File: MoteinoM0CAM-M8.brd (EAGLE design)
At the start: 22.6 x 22.2 mm, 9 parts

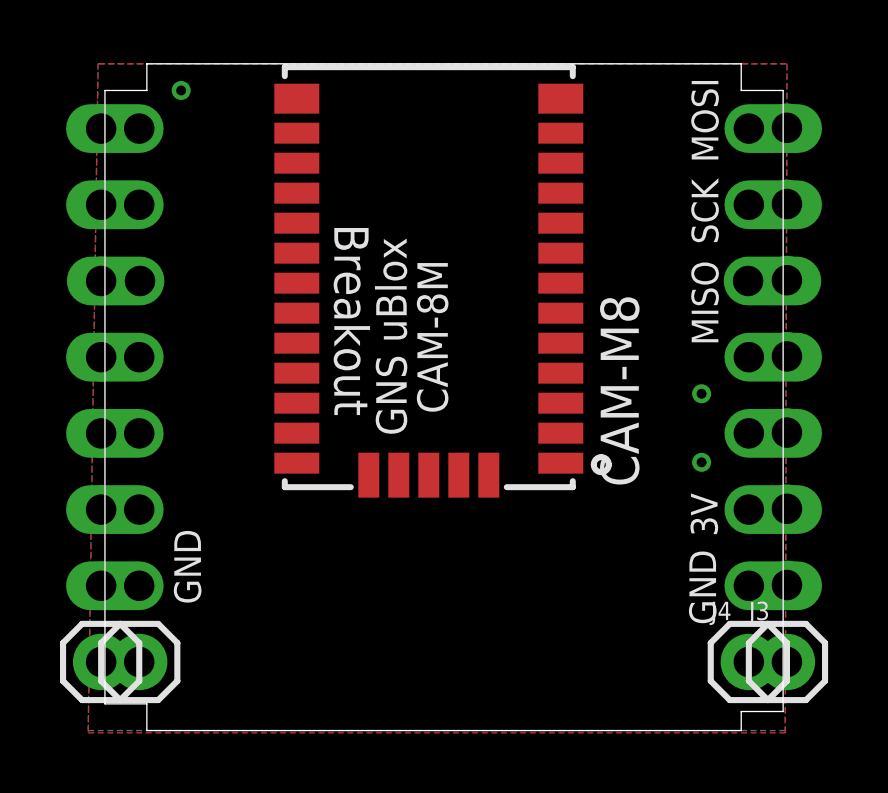
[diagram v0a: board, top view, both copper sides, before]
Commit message: Added resistors, led and capacitors
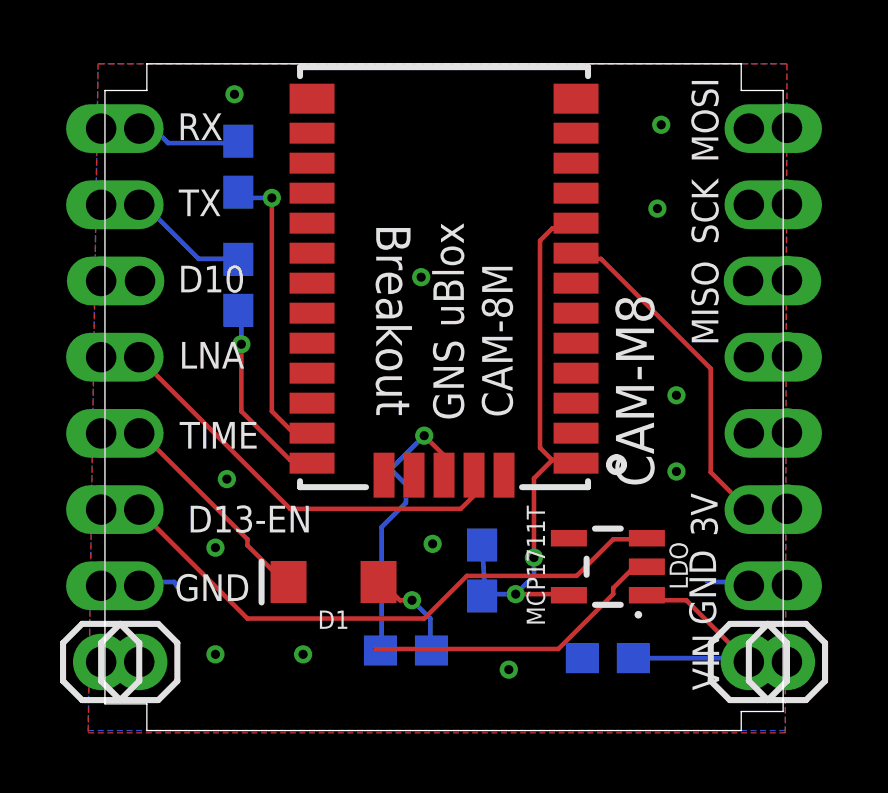
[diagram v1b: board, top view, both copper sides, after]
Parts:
- added C1, C2: 100n, SparkFun-Capacitors:0603
- added D1: GREEN, SparkFun-LED:LED-1206
- added LDO: MCP1711T, SparkFun-IC-Power:SOT23-5
- added R1, R2, R3: 220, SparkFun-Resistors:0603
- moved U$1 0.51 mm to (11.4, 13.2)
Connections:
- removed net D11: U$17.4
- removed net D12: U$17.3
- removed net D13: U$17.2
- new net D11_LNA_EN: U$1.30, U$17.4
- new net D12_TIMEPULSE: D1.C, U$17.3
- new net D13_ENABLE: LDO.3, U$17.2
- new net N$1: R3.2, U$1.29
- new net N$3: R2.2, U$1.26
- new net N$4: D1.A, R3.1
- new net VCC: C2.1, LDO.5, U$1.1, U$1.9
- net GND: now also C1.2, C2.2, LDO.2
- net N$2: now also R1.2, U$1.25; no longer U$1.1, U$1.9
- net PB22/TXD: now also R2.1
- net PB23/RXD: now also R1.1
- net VIN: now also C1.1, LDO.1
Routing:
- net D13_ENABLE: track 0.00 -> 19.5 mm
- net VCC: track 0.00 -> 19.2 mm, vias 0 -> 2
- net D11_LNA_EN: track 0.00 -> 14.1 mm
- net GND: track 0.00 -> 13.5 mm, vias 3 -> 12
- net 3.3V: track 0.00 -> 11.4 mm
- net N$1: track 0.00 -> 10.3 mm, vias 0 -> 1
- net N$2: track 0.00 -> 9.99 mm, vias 0 -> 1
- net VIN: track 0.00 -> 8.47 mm
- net D12_TIMEPULSE: track 0.00 -> 7.13 mm
- net N$3: track 0.00 -> 6.47 mm, vias 0 -> 1
- net PB22/TXD: track 0.00 -> 4.06 mm
- net PB23/RXD: track 0.00 -> 3.51 mm
- net N$4: track 0.00 -> 3.31 mm, vias 0 -> 1
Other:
- board text added: "D10"
- board text added: "D13-EN"
- board text added: "LNA"
- board text added: "RX"
- board text added: "TIME"
- board text added: "TX"
- board text added: "VIN"

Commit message: Doco update III
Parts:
- C1, C2: value 100n -> 100nF
- moved D1 3.74 mm to (5.59, 0.00)
- moved R3 2.88 mm to (8.00, 2.67), flipped to the top
- moved C2 0.76 mm to (12.7, 2.67), flipped to the top
- moved C1 0.51 mm to (16.9, 0.00), flipped to the top
- moved LDO 0.51 mm to (16.9, 3.05)
- flipped R1 to the top
- flipped R2 to the top
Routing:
- net GND: track 13.5 -> 23.9 mm, vias 12 -> 0
- net D13_ENABLE: track 19.5 -> 25.3 mm
- net N$1: track 10.3 -> 4.98 mm, vias 1 -> 0
- net D12_TIMEPULSE: track 7.13 -> 9.21 mm
- net VCC: track 19.2 -> 17.5 mm, vias 2 -> 0
- net VIN: track 8.47 -> 7.11 mm
- net N$4: track 3.31 -> 2.71 mm, vias 1 -> 0
- net N$2: track 9.99 -> 9.39 mm, vias 1 -> 0
- net N$3: vias 1 -> 0
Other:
- board text added: "CAM-M8Q"
- board text removed: "CAM-M8"

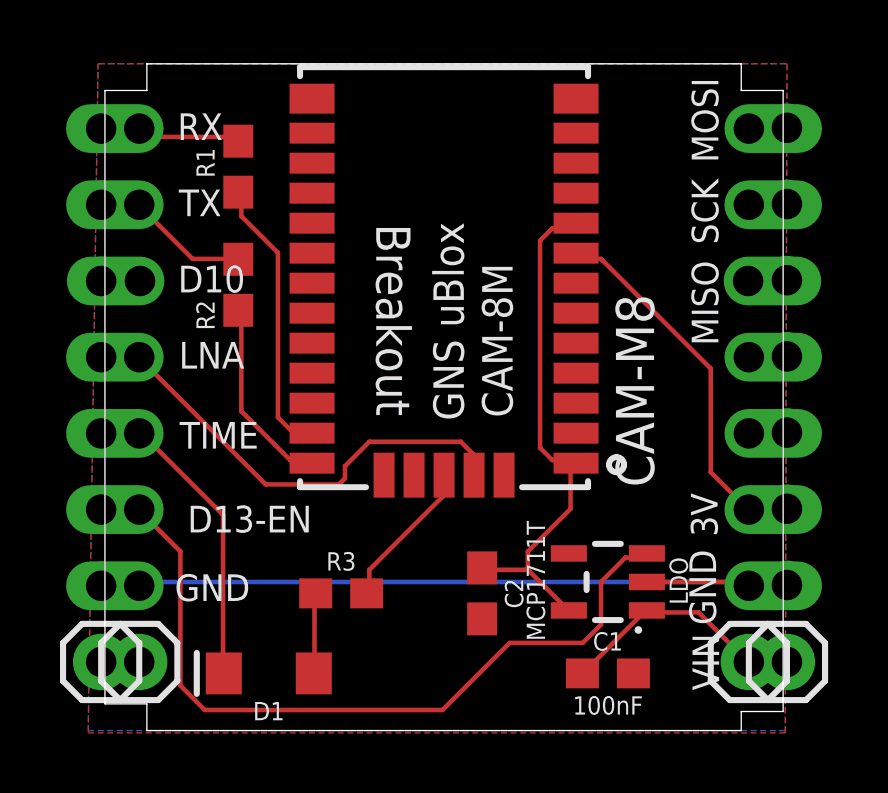
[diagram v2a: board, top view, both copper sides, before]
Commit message: Added images
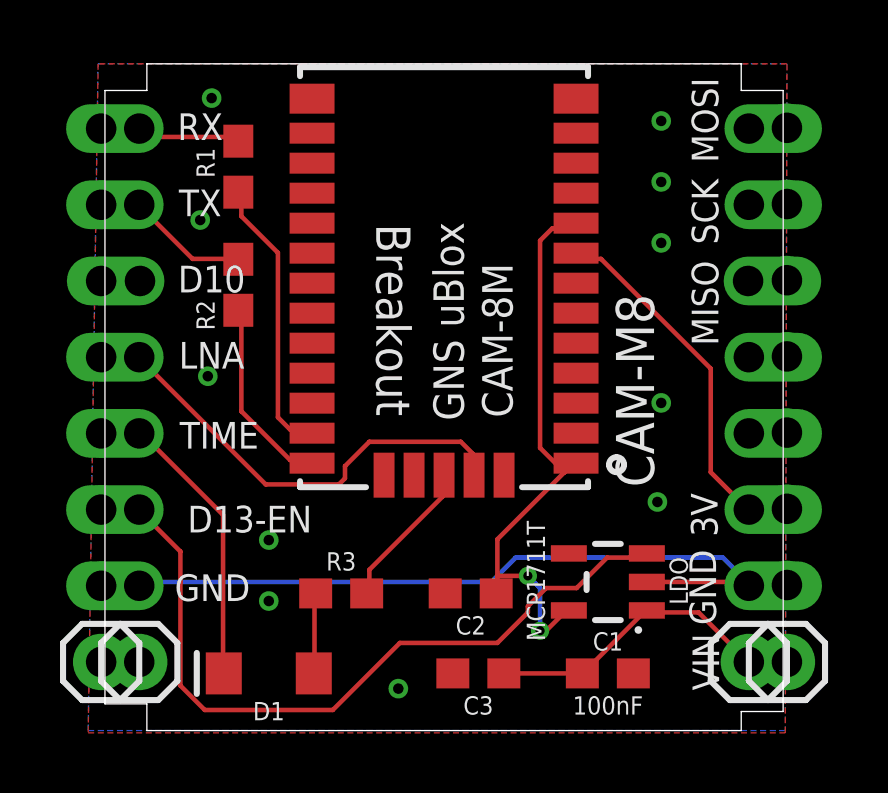
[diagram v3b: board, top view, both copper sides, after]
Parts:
- added C3: 4.7uF, SparkFun-Capacitors:0603
- moved C2 0.38 mm to (12.3, 2.67), turned to 180 degrees
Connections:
- net GND: now also C3.2
- net VIN: now also C3.1
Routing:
- net VIN: track 7.11 -> 9.73 mm
- net VCC: track 17.5 -> 19.7 mm, vias 0 -> 2
- net D13_ENABLE: track 25.3 -> 24.6 mm
- net GND: track 23.9 -> 24.6 mm, vias 0 -> 11
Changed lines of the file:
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@@
 <attribute name="VALUE" x="16.891" y="-0.762" size="0.6096" layer="25" font="vector" ratio="20" align="top-center"/>
 </element>
-<element name="C2" library="SparkFun-Capacitors" library_urn="urn:adsk.eagle:library:510" package="0603" package3d_urn="urn:adsk.eagle:package:37414/1" value="100nF" x="12.7" y="2.667" smashed="yes" rot="R270">
-<attribute name="NAME" x="13.462" y="2.667" size="0.6096" layer="25" font="vector" ratio="20" rot="R270" align="bottom-center"/>
-<attribute name="PROD_ID" value="CAP-08604" x="12.7" y="2.667" size="1.778" layer="27" rot="R270" display="off"/>
-<attribute name="VALUE" x="11.938" y="2.667" size="0.6096" layer="27" font="vector" ratio="20" rot="R270" align="top-center"/>
+<element name="C2" library="SparkFun-Capacitors" library_urn="urn:adsk.eagle:library:510" package="0603" package3d_urn="urn:adsk.eagle:package:37414/1" value="100nF" x="12.319" y="2.667" smashed="yes" rot="R180">
+<attribute name="NAME" x="12.319" y="1.905" size="0.6096" layer="25" font="vector" ratio="20" rot="R180" align="bottom-center"/>
+<attribute name="PROD_ID" value="CAP-08604" x="12.319" y="2.667" size="1.778" layer="27" rot="R180" display="off"/>
+<attribute name="VALUE" x="12.319" y="3.429" size="0.6096" layer="27" font="vector" ratio="20" rot="R180" align="top-center"/>
 </element>
 <element name="D1" library="SparkFun-LED" library_urn="urn:adsk.eagle:library:529" package="LED-1206" package3d_urn="urn:adsk.eagle:package:39352/1" value="GREEN" x="5.588" y="0" smashed="yes" rot="R180">
@@
 <attribute name="PROD_ID" value="RES-07861" x="8.001" y="2.667" size="1.778" layer="27" display="off"/>
 <attribute name="VALUE" x="8.001" y="1.905" size="0.6096" layer="27" font="vector" ratio="20" align="top-center"/>
+</element>
+<element name="C3" library="SparkFun-Capacitors" library_urn="urn:adsk.eagle:library:510" package="0603" package3d_urn="urn:adsk.eagle:package:37414/1" value="4.7uF" x="12.573" y="0" smashed="yes" rot="R180">
+<attribute name="NAME" x="12.573" y="-0.762" size="0.6096" layer="25" font="vector" ratio="20" rot="R180" align="bottom-center"/>
+<attribute name="PROD_ID" value="CAP-08280" x="12.573" y="0" size="1.778" layer="27" rot="R180" display="off"/>
+<attribute name="VALUE" x="12.573" y="0.762" size="0.6096" layer="27" font="vector" ratio="20" rot="R180" align="top-center"/>
 </element>
 </elements>
@@
 <contactref element="C2" pad="2"/>
 <contactref element="U$18" pad="1"/>
-<wire x1="21.5392" y1="3.048" x2="1.4224" y2="3.048" width="0.1524" layer="16"/>
+<contactref element="C3" pad="2"/>
+<wire x1="13.0048" y1="3.048" x2="1.4224" y2="3.048" width="0.1524" layer="16"/>
+<wire x1="13.8176" y1="3.8608" x2="13.0048" y2="3.048" width="0.1524" layer="16"/>
+<wire x1="20.7264" y1="3.8608" x2="13.8176" y2="3.8608" width="0.1524" layer="16"/>
+<wire x1="21.5392" y1="3.048" x2="20.7264" y2="3.8608" width="0.1524" layer="16"/>
 <wire x1="1.4224" y1="3.048" x2="1.27" y2="2.921" width="0.1524" layer="16"/>
 <wire x1="21.5392" y1="3.048" x2="21.59" y2="2.921" width="0.1524" layer="16"/>
 <wire x1="18.1911" y1="3.048" x2="21.5392" y2="3.048" width="0.1524" layer="1"/>
 <wire x1="21.5392" y1="3.048" x2="21.59" y2="2.921" width="0.1524" layer="1"/>
-<wire x1="13.43" y1="6.608" x2="9.43" y2="6.608" width="0" layer="19" extent="1-1"/>
-<wire x1="15.83" y1="10.008" x2="13.43" y2="6.608" width="0" layer="19" extent="1-1"/>
-<wire x1="17.741" y1="0" x2="18.1911" y2="3.048" width="0" layer="19" extent="1-1"/>
-<wire x1="15.83" y1="16.008" x2="15.83" y2="11.008" width="0" layer="19" extent="1-1"/>
+<via x="3.683" y="19.177" extent="1-16" drill="0.35"/>
+<via x="3.302" y="15.113" extent="1-16" drill="0.35"/>
+<via x="3.556" y="9.906" extent="1-16" drill="0.35"/>
+<via x="5.588" y="4.445" extent="1-16" drill="0.35"/>
+<via x="5.588" y="2.413" extent="1-16" drill="0.35"/>
+<via x="9.906" y="-0.508" extent="1-16" drill="0.35"/>
+<via x="18.542" y="5.715" extent="1-16" drill="0.35"/>
+<via x="18.669" y="9.017" extent="1-16" drill="0.35"/>
+<via x="18.669" y="14.351" extent="1-16" drill="0.35"/>
+<via x="18.669" y="16.383" extent="1-16" drill="0.35"/>
+<via x="18.669" y="18.415" extent="1-16" drill="0.35"/>
+<wire x1="18.669" y1="16.383" x2="18.669" y2="18.415" width="0" layer="19" extent="1-1"/>
+<wire x1="11.469" y1="2.667" x2="13.0048" y2="3.048" width="0" layer="19" extent="1-16"/>
 </signal>
 <signal name="SDA">
@@
 <contactref element="LDO" pad="1"/>
 <contactref element="C1" pad="1"/>
-<wire x1="18.0848" y1="2.032" x2="16.0528" y2="0" width="0.1524" layer="1"/>
+<contactref element="C3" pad="1"/>
+<wire x1="16.041" y1="0" x2="13.423" y2="0" width="0.1524" layer="1"/>
+<wire x1="16.0528" y1="0" x2="18.0848" y2="2.032" width="0.1524" layer="1"/>
+<wire x1="18.0848" y1="2.032" x2="18.1911" y2="2.098" width="0.1524" layer="1"/>
 <wire x1="16.0528" y1="0" x2="16.041" y2="0" width="0.1524" layer="1"/>
-<wire x1="18.0848" y1="2.032" x2="18.1911" y2="2.098" width="0.1524" layer="1"/>
 <wire x1="19.9136" y1="2.032" x2="18.288" y2="2.032" width="0.1524" layer="1"/>
 <wire x1="21.5392" y1="0.4064" x2="19.9136" y2="2.032" width="0.1524" layer="1"/>
@@
 <contactref element="LDO" pad="3"/>
 <contactref element="U$17" pad="2"/>
-<wire x1="17.4752" y1="3.8608" x2="18.0848" y2="3.8608" width="0.1524" layer="1"/>
-<wire x1="16.6624" y1="3.048" x2="17.4752" y2="3.8608" width="0.1524" layer="1"/>
-<wire x1="16.6624" y1="1.6256" x2="16.6624" y2="3.048" width="0.1524" layer="1"/>
-<wire x1="16.0528" y1="1.016" x2="16.6624" y2="1.6256" width="0.1524" layer="1"/>
-<wire x1="13.6144" y1="1.016" x2="16.0528" y2="1.016" width="0.1524" layer="1"/>
-<wire x1="11.3792" y1="-1.2192" x2="13.6144" y2="1.016" width="0.1524" layer="1"/>
-<wire x1="3.4544" y1="-1.2192" x2="11.3792" y2="-1.2192" width="0.1524" layer="1"/>
+<wire x1="16.8656" y1="3.8608" x2="18.0848" y2="3.8608" width="0.1524" layer="1"/>
+<wire x1="15.8496" y1="2.8448" x2="16.8656" y2="3.8608" width="0.1524" layer="1"/>
+<wire x1="14.8336" y1="2.8448" x2="15.8496" y2="2.8448" width="0.1524" layer="1"/>
+<wire x1="14.224" y1="2.2352" x2="14.8336" y2="2.8448" width="0.1524" layer="1"/>
+<wire x1="14.224" y1="2.032" x2="14.224" y2="2.2352" width="0.1524" layer="1"/>
+<wire x1="13.208" y1="1.016" x2="14.224" y2="2.032" width="0.1524" layer="1"/>
+<wire x1="9.9568" y1="1.016" x2="13.208" y2="1.016" width="0.1524" layer="1"/>
+<wire x1="7.7216" y1="-1.2192" x2="9.9568" y2="1.016" width="0.1524" layer="1"/>
+<wire x1="3.4544" y1="-1.2192" x2="7.7216" y2="-1.2192" width="0.1524" layer="1"/>
 <wire x1="2.6416" y1="-0.4064" x2="3.4544" y2="-1.2192" width="0.1524" layer="1"/>
 <wire x1="2.6416" y1="4.064" x2="2.6416" y2="-0.4064" width="0.1524" layer="1"/>
@@
 <contactref element="C2" pad="1"/>
 <contactref element="LDO" pad="5"/>
-<wire x1="14.224" y1="3.4544" x2="12.8016" y2="3.4544" width="0.1524" layer="1"/>
-<wire x1="15.4432" y1="2.2352" x2="14.224" y2="3.4544" width="0.1524" layer="1"/>
-<wire x1="12.8016" y1="3.4544" x2="12.7" y2="3.517" width="0.1524" layer="1"/>
-<wire x1="15.4432" y1="2.2352" x2="15.5909" y2="2.098" width="0.1524" layer="1"/>
-<wire x1="15.6464" y1="5.4864" x2="15.6464" y2="6.9088" width="0.1524" layer="1"/>
-<wire x1="14.224" y1="4.064" x2="15.6464" y2="5.4864" width="0.1524" layer="1"/>
-<wire x1="14.224" y1="3.4544" x2="14.224" y2="4.064" width="0.1524" layer="1"/>
+<wire x1="13.208" y1="4.4704" x2="13.208" y2="3.2512" width="0.1524" layer="1"/>
+<wire x1="13.208" y1="3.2512" x2="13.208" y2="2.8448" width="0.1524" layer="1"/>
+<wire x1="15.6464" y1="6.9088" x2="15.4432" y2="6.7056" width="0.1524" layer="1"/>
+<wire x1="15.4432" y1="6.7056" x2="13.208" y2="4.4704" width="0.1524" layer="1"/>
+<wire x1="13.208" y1="2.8448" x2="13.169" y2="2.667" width="0.1524" layer="1"/>
 <wire x1="15.6464" y1="6.9088" x2="15.83" y2="7.008" width="0.1524" layer="1"/>
+<wire x1="14.8336" y1="1.4224" x2="15.4432" y2="2.032" width="0.1524" layer="1"/>
+<wire x1="14.6304" y1="1.4224" x2="14.8336" y2="1.4224" width="0.1524" layer="1"/>
+<wire x1="14.6304" y1="2.8448" x2="14.6304" y2="1.4224" width="0.1524" layer="16"/>
+<wire x1="14.224" y1="3.2512" x2="14.6304" y2="2.8448" width="0.1524" layer="16"/>
+<wire x1="13.208" y1="3.2512" x2="14.224" y2="3.2512" width="0.1524" layer="1"/>
+<wire x1="15.4432" y1="2.032" x2="15.5909" y2="2.098" width="0.1524" layer="1"/>
 <wire x1="15.0368" y1="14.8336" x2="15.6464" y2="14.8336" width="0.1524" layer="1"/>
 <wire x1="14.6304" y1="14.4272" x2="15.0368" y2="14.8336" width="0.1524" layer="1"/>
 <wire x1="14.6304" y1="7.5184" x2="14.6304" y2="14.4272" width="0.1524" layer="1"/>
-<wire x1="15.0368" y1="7.112" x2="14.6304" y2="7.5184" width="0.1524" layer="1"/>
-<wire x1="15.6464" y1="7.112" x2="15.0368" y2="7.112" width="0.1524" layer="1"/>
+<wire x1="15.4432" y1="6.7056" x2="14.6304" y2="7.5184" width="0.1524" layer="1"/>
 <wire x1="15.6464" y1="14.8336" x2="15.83" y2="15.008" width="0.1524" layer="1"/>
-<wire x1="15.6464" y1="7.112" x2="15.83" y2="7.008" width="0.1524" layer="1"/>
+<wire x1="15.4432" y1="6.7056" x2="15.83" y2="7.008" width="0.1524" layer="1"/>
+<via x="14.6304" y="1.4224" extent="1-16" drill="0.3048"/>
+<via x="14.224" y="3.2512" extent="1-16" drill="0.3048"/>
 </signal>
 <signal name="VCC1">

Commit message: added vias
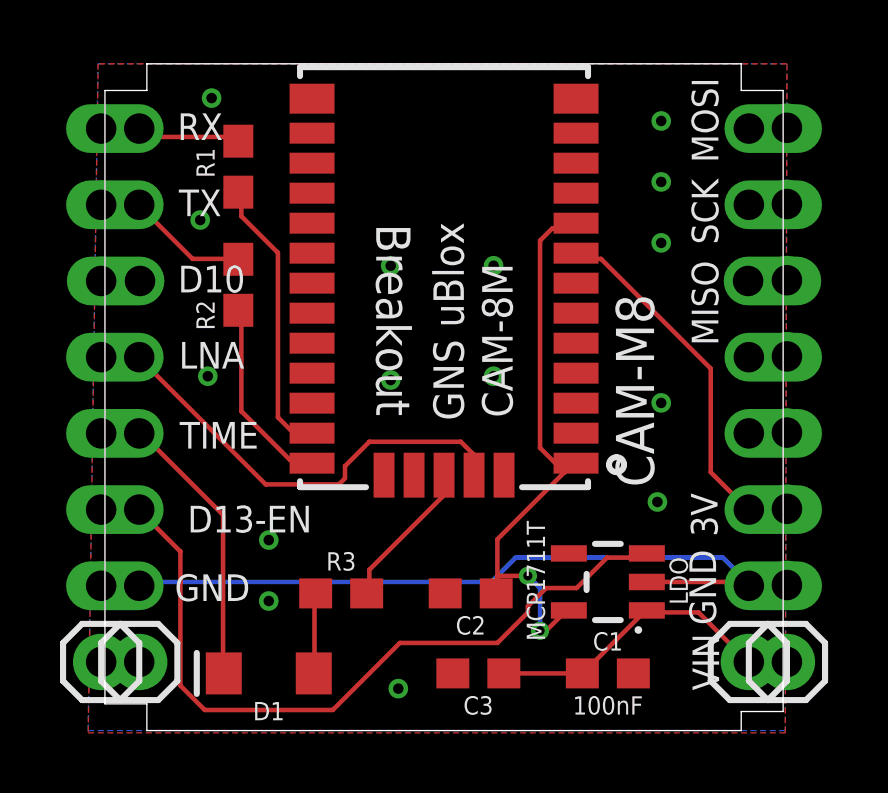
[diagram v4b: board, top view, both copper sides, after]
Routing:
- net GND: vias 11 -> 15
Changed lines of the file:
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@@
 <wire x1="18.669" y1="16.383" x2="18.669" y2="18.415" width="0" layer="19" extent="1-1"/>
 <wire x1="11.469" y1="2.667" x2="13.0048" y2="3.048" width="0" layer="19" extent="1-16"/>
+<via x="13.081" y="13.589" extent="1-16" drill="0.35"/>
+<via x="9.652" y="13.589" extent="1-16" drill="0.35"/>
+<via x="13.081" y="9.906" extent="1-16" drill="0.35"/>
+<via x="9.652" y="9.779" extent="1-16" drill="0.35"/>
 </signal>
 <signal name="SDA">

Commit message: Connection tidy, layout tweaks
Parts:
- moved C2 0.38 mm to (12.3, 3.05)
- moved R3 0.38 mm to (8.00, 3.05)
- moved C3 0.25 mm to (12.3, 0.00)
- moved C1 0.13 mm to (17.0, 0.00)
- moved R1 0.13 mm to (4.45, 16.9)
- moved R2 0.13 mm to (4.45, 13.0)
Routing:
- net GND: track 24.6 -> 25.0 mm, vias 15 -> 21

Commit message: updates
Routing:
- net D13_ENABLE: track 24.5 -> 18.0 mm, vias 0 -> 1
- net GND: track 25.0 -> 21.9 mm, vias 21 -> 22
- net D11_LNA_EN: track 14.6 -> 13.2 mm, vias 0 -> 1
- net VCC: track 19.9 -> 18.8 mm, vias 2 -> 0
- net VIN: track 10.1 -> 10.7 mm
- net 3.3V: vias 0 -> 1
